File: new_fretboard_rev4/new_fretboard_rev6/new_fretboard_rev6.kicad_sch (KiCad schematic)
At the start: 0 parts

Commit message: two channels done
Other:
- added sheet ch2 (../new_fretboard_rev4/new_fretboard_rev4.kicad_sch)
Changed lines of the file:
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@@
 	(paper "A4")
 	(sheet
-		(at 54.61 27.94)
-		(size 25.4 17.78)
+		(at 29.21 27.94)
+		(size 22.86 13.97)
 		(exclude_from_sim no)
 		(in_bom yes)
@@
 		)
 		(property "Sheetname" "ch1"
-			(at 54.61 27.2284 0)
+			(at 29.21 27.2284 0)
 			(show_name no)
 			(do_not_autoplace no)
@@
 		)
 		(property "Sheetfile" "../new_fretboard_rev4/new_fretboard_rev4.kicad_sch"
-			(at 54.61 46.3046 0)
+			(at 29.21 42.4946 0)
 			(show_name no)
 			(do_not_autoplace no)
@@
 				)
 			)
+		)
+	)
+	(sheet
+		(at 99.06 25.4)
+		(size 31.75 16.51)
+		(exclude_from_sim no)
+		(in_bom yes)
+		(on_board yes)
+		(dnp no)
+		(fields_autoplaced yes)
+		(stroke
+			(width 0.1524)
+			(type solid)
+		)
+		(fill
+			(color 0 0 0 0)
+		)
+		(property "Sheetname" "ch2"
+			(at 99.06 24.6884 0)
+			(show_name no)
+			(do_not_autoplace no)
+			(effects
+				(font
+					(size 1.27 1.27)
+				)
+				(justify left bottom)
+			)
+		)
+		(property "Sheetfile" "../new_fretboard_rev4/new_fretboard_rev4.kicad_sch"
+			(at 99.06 42.4946 0)
+			(show_name no)
+			(do_not_autoplace no)
+			(effects
+				(font
+					(size 1.27 1.27)
+				)
+				(justify left top)
+			)
+		)
+		(instances
+			(project "new_fretboard_rev6"
+				(path "/0062b2a7-78dc-4b3a-83d1-c8e3134dc888"
+					(page "3")
+				)
+			)

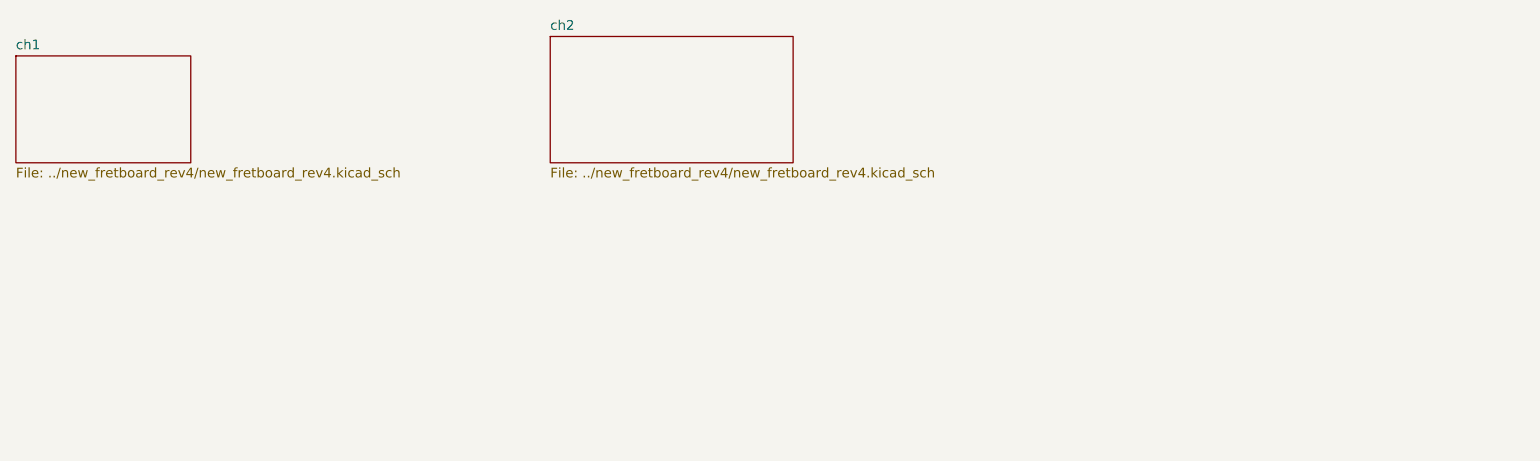
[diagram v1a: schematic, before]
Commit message: fully routed all channels, about to add tilts
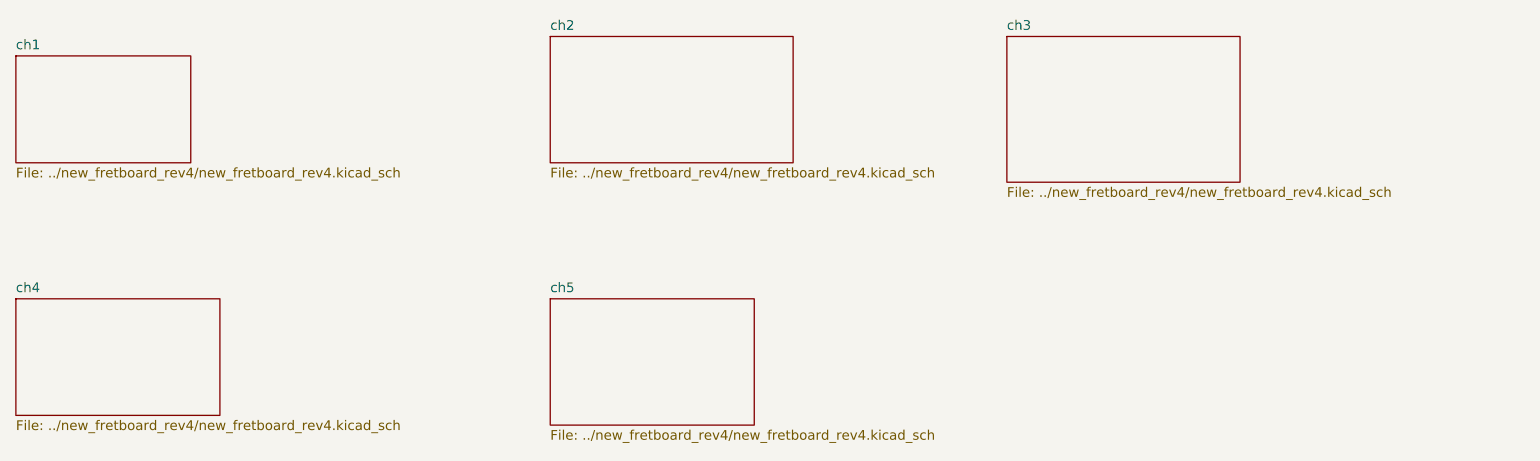
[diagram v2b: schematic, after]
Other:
- added sheet ch3 (../new_fretboard_rev4/new_fretboard_rev4.kicad_sch)
- added sheet ch4 (../new_fretboard_rev4/new_fretboard_rev4.kicad_sch)
- added sheet ch5 (../new_fretboard_rev4/new_fretboard_rev4.kicad_sch)
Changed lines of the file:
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@@
 	(paper "A4")
+	(sheet
+		(at 99.06 59.69)
+		(size 26.67 16.51)
+		(exclude_from_sim no)
+		(in_bom yes)
+		(on_board yes)
+		(dnp no)
+		(fields_autoplaced yes)
+		(stroke
+			(width 0.1524)
+			(type solid)
+		)
+		(fill
+			(color 0 0 0 0)
+		)
+		(property "Sheetname" "ch5"
+			(at 99.06 58.9784 0)
+			(show_name no)
+			(do_not_autoplace no)
+			(effects
+				(font
+					(size 1.27 1.27)
+				)
+				(justify left bottom)
+			)
+		)
+		(property "Sheetfile" "../new_fretboard_rev4/new_fretboard_rev4.kicad_sch"
+			(at 99.06 76.7846 0)
+			(show_name no)
+			(do_not_autoplace no)
+			(effects
+				(font
+					(size 1.27 1.27)
+				)
+				(justify left top)
+			)
+		)
+		(instances
+			(project "new_fretboard_rev6"
+				(path "/0062b2a7-78dc-4b3a-83d1-c8e3134dc888"
+					(page "6")
+				)
+			)
+		)
+	)
+	(sheet
+		(at 29.21 59.69)
+		(size 26.67 15.24)
+		(exclude_from_sim no)
+		(in_bom yes)
+		(on_board yes)
+		(dnp no)
+		(fields_autoplaced yes)
+		(stroke
+			(width 0.1524)
+			(type solid)
+		)
+		(fill
+			(color 0 0 0 0)
+		)
+		(property "Sheetname" "ch4"
+			(at 29.21 58.9784 0)
+			(show_name no)
+			(do_not_autoplace no)
+			(effects
+				(font
+					(size 1.27 1.27)
+				)
+				(justify left bottom)
+			)
+		)
+		(property "Sheetfile" "../new_fretboard_rev4/new_fretboard_rev4.kicad_sch"
+			(at 29.21 75.5146 0)
+			(show_name no)
+			(do_not_autoplace no)
+			(effects
+				(font
+					(size 1.27 1.27)
+				)
+				(justify left top)
+			)
+		)
+		(instances
+			(project "new_fretboard_rev6"
+				(path "/0062b2a7-78dc-4b3a-83d1-c8e3134dc888"
+					(page "5")
+				)
+			)
+		)
+	)
+	(sheet
+		(at 158.75 25.4)
+		(size 30.48 19.05)
+		(exclude_from_sim no)
+		(in_bom yes)
+		(on_board yes)
+		(dnp no)
+		(fields_autoplaced yes)
+		(stroke
+			(width 0.1524)
+			(type solid)
+		)
+		(fill
+			(color 0 0 0 0)
+		)
+		(property "Sheetname" "ch3"
+			(at 158.75 24.6884 0)
+			(show_name no)
+			(do_not_autoplace no)
+			(effects
+				(font
+					(size 1.27 1.27)
+				)
+				(justify left bottom)
+			)
+		)
+		(property "Sheetfile" "../new_fretboard_rev4/new_fretboard_rev4.kicad_sch"
+			(at 158.75 45.0346 0)
+			(show_name no)
+			(do_not_autoplace no)
+			(effects
+				(font
+					(size 1.27 1.27)
+				)
+				(justify left top)
+			)
+		)
+		(instances
+			(project "new_fretboard_rev6"
+				(path "/0062b2a7-78dc-4b3a-83d1-c8e3134dc888"
+					(page "4")
+				)
+			)
+		)
+	)
 	(sheet
 		(at 29.21 27.94)

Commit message: channels are done, working on microcontroller, daisy, and power junctions. getting heirarchical pin stuff sorted.
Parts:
- added J11: Conn_01x02_Pin, Connector_PinHeader_2.54mm:PinHeader_1x02_P2.54mm_Vertical, symbol Connector:Conn_01x02_Pin
- added J?: 110990030, Snapeda:SEEED_110990030, symbol Snapeda:110990030
- added U10: Daisy_Seed3, Module:Electrosmith_Daisy_Seed, symbol Snapeda:Daisy_Seed3
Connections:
- new net +5V: J?.1, J?.2
- new net GND1: J?.3, J?.4

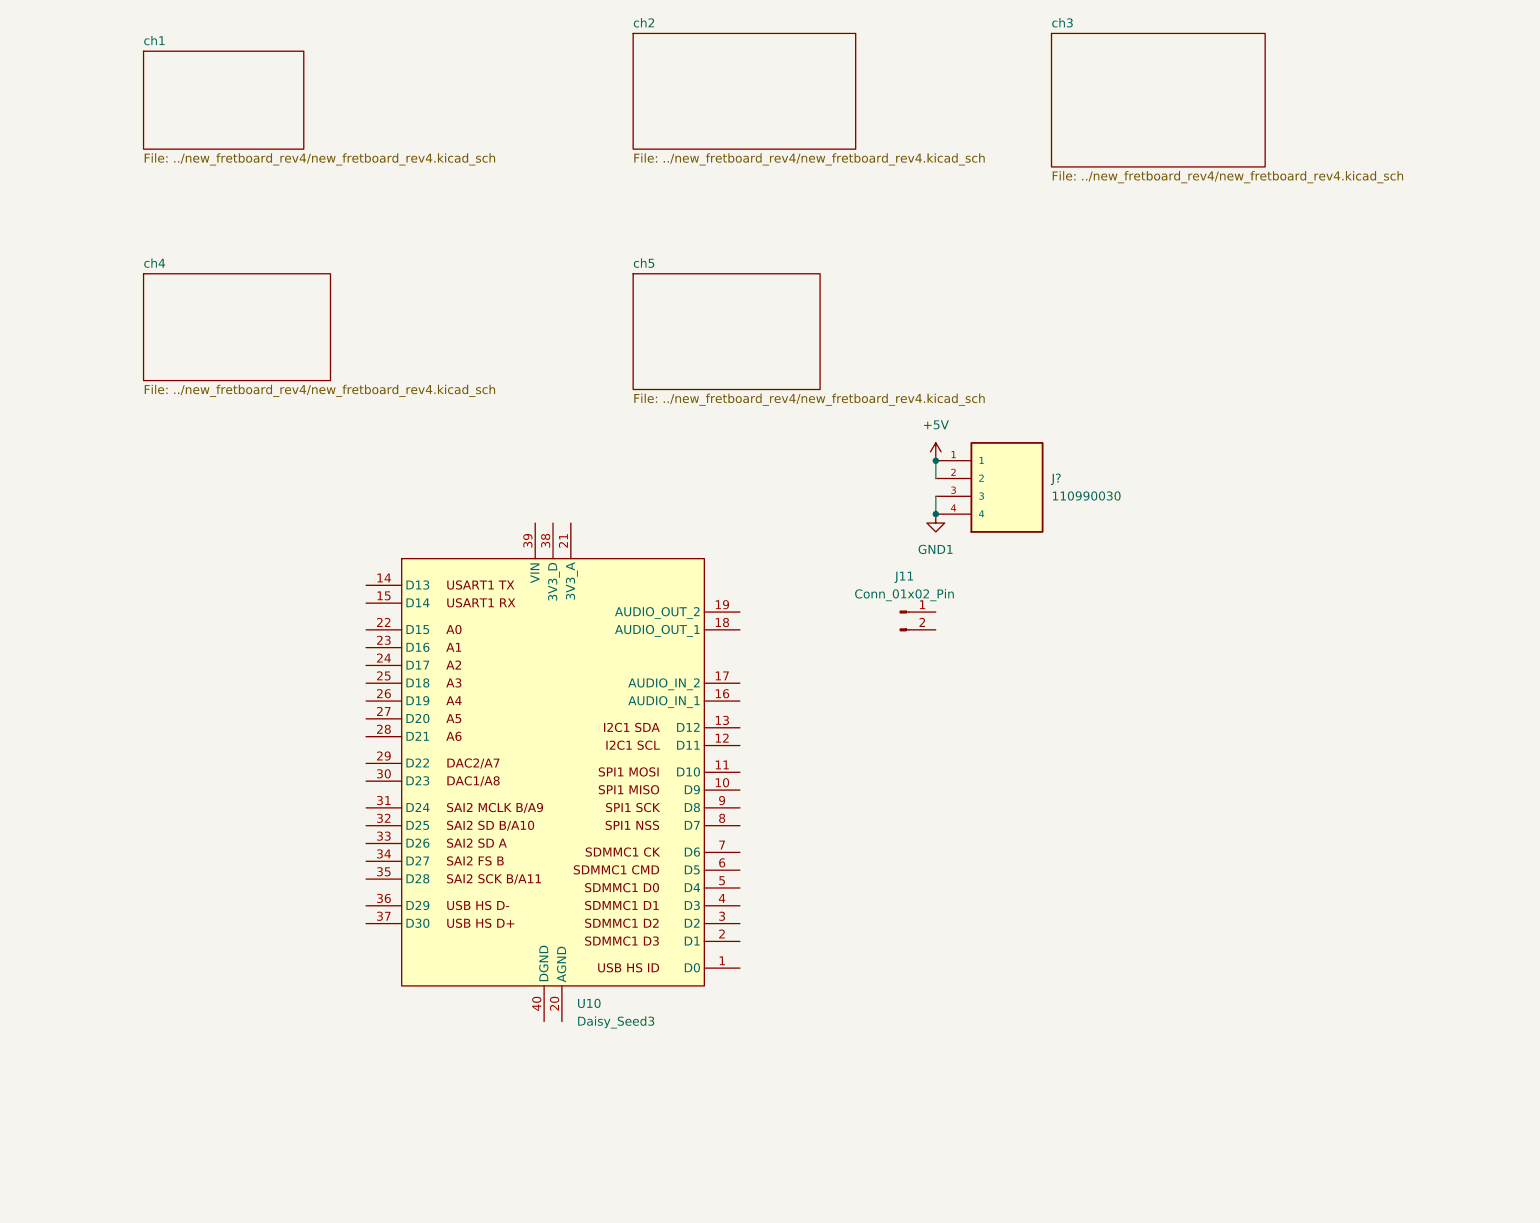
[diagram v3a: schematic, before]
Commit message: power in schematic, about to route power and sent wires
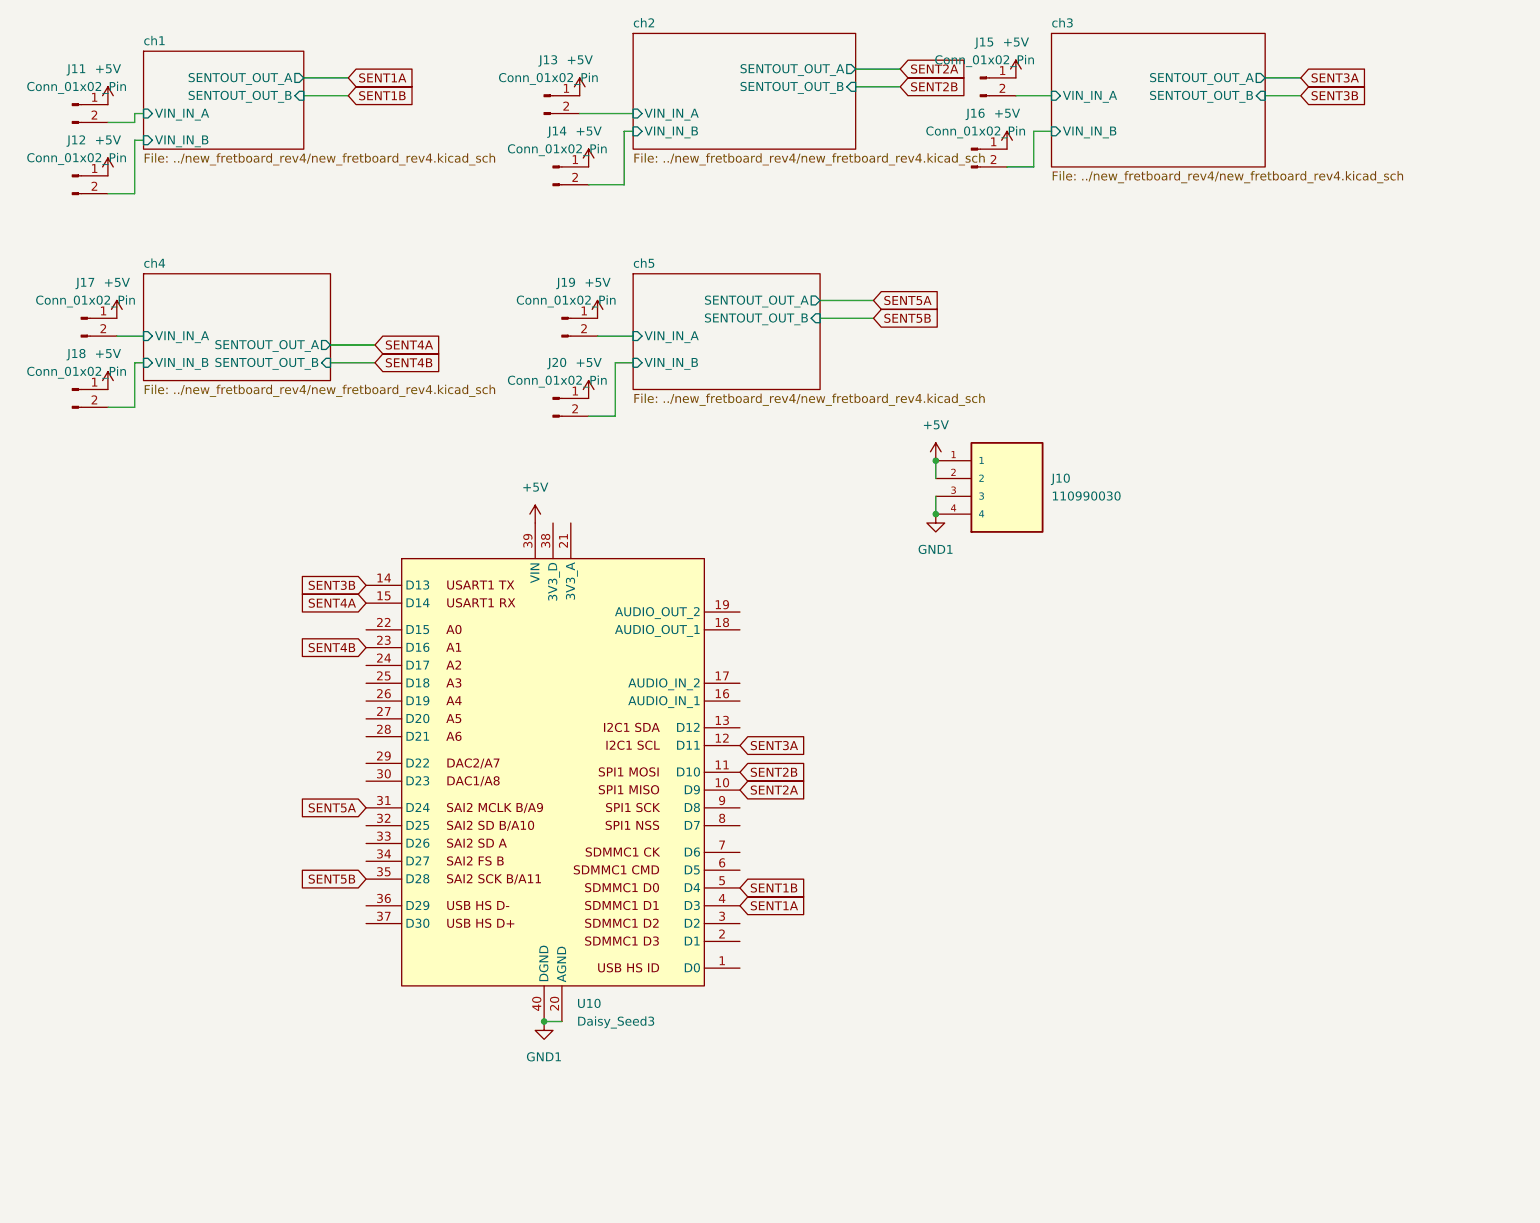
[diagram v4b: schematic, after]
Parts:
- added J12, J13, J14, J15, J16, J17, J18, J19, J20: Conn_01x02_Pin, Connector_PinHeader_2.54mm:PinHeader_1x02_P2.54mm_Vertical, symbol Connector:Conn_01x02_Pin
- gave numbers to parts that had none: 1
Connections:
- net +5V: now also J11.1 (Pin_1), U10.39 (VIN), J12.1 (Pin_1), J13.1 (Pin_1), J14.1 (Pin_1), J15.1 (Pin_1), J16.1 (Pin_1), J17.1 (Pin_1), J18.1 (Pin_1), J19.1 (Pin_1), J20.1 (Pin_1)
- net GND1: now also U10.20 (AGND), U10.40 (DGND)
- net SENT2A: now reaches U10.10 (D9)
- net SENT2B: now reaches U10.11 (D10)
- net SENT3A: now reaches U10.12 (D11)
- net SENT3B: now reaches U10.14 (D13)
- net SENT4A: now reaches U10.15 (D14)
- net SENT4B: now reaches U10.23 (D16)
- net SENT5A: now reaches U10.31 (D24)
- net SENT5B: now reaches U10.35 (D28)
- net SENT1A: now reaches U10.4 (D3)
- net SENT1B: now reaches U10.5 (D4)
- net ch1/VIN_IN_A: now reaches J11.2 (Pin_2)
- new net ch1/VIN_IN_B: J12.2 (Pin_2)
- new net ch2/VIN_IN_A: J13.2 (Pin_2)
- new net ch2/VIN_IN_B: J14.2 (Pin_2)
- new net ch3/VIN_IN_A: J15.2 (Pin_2)
- new net ch3/VIN_IN_B: J16.2 (Pin_2)
- new net ch4/VIN_IN_A: J17.2 (Pin_2)
- new net ch4/VIN_IN_B: J18.2 (Pin_2)
- new net ch5/VIN_IN_A: J19.2 (Pin_2)
- new net ch5/VIN_IN_B: J20.2 (Pin_2)
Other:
- sheet ch1 ports: added SENTOUT_OUT_A, SENTOUT_OUT_B, VIN_IN_A, VIN_IN_B; removed none
- sheet ch2 ports: added SENTOUT_OUT_A, SENTOUT_OUT_B, VIN_IN_A, VIN_IN_B; removed none
- sheet ch3 ports: added SENTOUT_OUT_A, SENTOUT_OUT_B, VIN_IN_A, VIN_IN_B; removed none
- sheet ch4 ports: added SENTOUT_OUT_A, SENTOUT_OUT_B, VIN_IN_A, VIN_IN_B; removed none
- sheet ch5 ports: added SENTOUT_OUT_A, SENTOUT_OUT_B, VIN_IN_A, VIN_IN_B; removed none
- moved on the sheet: J11

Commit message: everything except cleaning up silkscreen done
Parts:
- added H1, H2: MountingHole, MountingHole:MountingHole_3.2mm_M3, symbol Mechanical:MountingHole
- added H3, H4, H5, H6, H7, H8, H9: MountingHole, MountingHole:MountingHole_2.1mm, symbol Mechanical:MountingHole
- added J24: Conn_01x03_Pin, Connector_PinHeader_2.54mm:PinHeader_1x03_P2.54mm_Vertical, symbol Connector:Conn_01x03_Pin
- added J25: Conn_01x07_Pin, Connector_PinHeader_2.54mm:PinHeader_1x07_P2.54mm_Vertical, symbol Connector:Conn_01x07_Pin
- added J26: Conn_01x01_Pin, Connector_PinSocket_2.54mm:PinSocket_1x01_P2.54mm_Vertical, symbol Connector:Conn_01x01_Pin
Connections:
- net at U10.1 (D0): now also J24.1 (Pin_1)
- net at U10.13 (D12): now also J26.1 (Pin_1)
- net at U10.2 (D1): now also J24.2 (Pin_2)
- net at U10.24 (D17): now also J25.1 (Pin_1)
- net at U10.25 (D18): now also J25.2 (Pin_2)
- net at U10.26 (D19): now also J25.3 (Pin_3)
- net at U10.27 (D20): now also J25.4 (Pin_4)
- net at U10.28 (D21): now also J25.5 (Pin_5)
- net at U10.29 (D22): now also J25.6 (Pin_6)
- net at U10.3 (D2): now also J24.3 (Pin_3)
- net at U10.30 (D23): now also J25.7 (Pin_7)

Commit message: finished, about to export gerbers
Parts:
- added J27: Conn_01x03_Pin, Connector_PinHeader_2.54mm:PinHeader_1x03_P2.54mm_Vertical, symbol Connector:Conn_01x03_Pin
- added J28: Conn_01x01_Pin, Connector_PinSocket_2.54mm:PinSocket_1x01_P2.54mm_Vertical, symbol Connector:Conn_01x01_Pin
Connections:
- net +5V: now also J27.3 (Pin_3)
- net GND1: now also J27.1 (Pin_1), J27.2 (Pin_2), J28.1 (Pin_1)

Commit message: all routing fixed, just added power cap
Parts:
- added C101: 22uf, Capacitor_THT:CP_Radial_D10.0mm_P3.50mm, symbol Device:C_Polarized
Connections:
- net +5V: now also C101.1
- net GND1: now also C101.2
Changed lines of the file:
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@@
 	(wire
 		(pts
+			(xy 138.43 86.36) (xy 142.24 86.36)
+		)
+		(stroke
+			(width 0)
+			(type default)
+		)
+	)
+	(wire
+		(pts
 			(xy 125.73 66.04) (xy 133.35 66.04)
 		)
@@
 	(wire
 		(pts
+			(xy 138.43 93.98) (xy 142.24 93.98)
+		)
+		(stroke
+			(width 0)
+			(type default)
+		)
+	)
+	(wire
+		(pts
 			(xy 156.21 39.37) (xy 158.75 39.37)
 		)
@@
 					(unit 1)
 				)
+			)
+		)
+	)
+	(symbol
+		(lib_id "Device:C_Polarized")
+		(at 138.43 90.17 0)
+		(unit 1)
+		(body_style 1)
+		(exclude_from_sim no)
+		(in_bom yes)
+		(on_board yes)
+		(in_pos_files yes)
+		(dnp no)
+		(property "Reference" "C101"
+			(at 130.302 89.662 0)
+			(show_name no)
+			(do_not_autoplace no)
+			(effects
+				(font
+					(size 1.27 1.27)
+				)
+				(justify left)
+			)
+		)
+		(property "Value" "22uf"
+			(at 130.81 87.63 0)
+			(show_name no)
+			(do_not_autoplace no)
+			(effects
+				(font
+					(size 1.27 1.27)
+				)
+				(justify left)
+			)
+		)
+		(property "Footprint" "Capacitor_THT:CP_Radial_D10.0mm_P3.50mm"
+			(at 139.3952 93.98 0)
+			(hide yes)
+			(show_name no)
+			(do_not_autoplace no)
+			(effects
+				(font
+					(size 1.27 1.27)
+				)
+			)
+		)
+		(property "Datasheet" ""
+			(at 138.43 90.17 0)
+			(hide yes)
+			(show_name no)
+			(do_not_autoplace no)
+			(effects
+				(font
+					(size 1.27 1.27)
+				)
+			)
+		)
+		(property "Description" "Polarized capacitor"
+			(at 138.43 90.17 0)
+			(hide yes)
+			(show_name no)
+			(do_not_autoplace no)
+			(effects
+				(font
+					(size 1.27 1.27)
+				)
+			)
+		)
+		(pin "2"
+		)
+		(pin "1"
+		)
+		(instances
+			(project "new_fretboard_rev6"
+				(path "/0062b2a7-78dc-4b3a-83d1-c8e3134dc888"
+					(reference "C101")
+					(unit 1)
+				)

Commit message: revision 6.1 finished
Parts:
- added C102: 1uf, Capacitor_SMD:C_1206_3216Metric, symbol Device:C
- C101: footprint Capacitor_THT:CP_Radial_D10.0mm_P3.50mm -> Capacitor_SMD:C_1210_3225Metric
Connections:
- net +5V: now also C102.1
- net GND1: now also C102.2
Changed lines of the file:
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@@
 	(paper "A4")
 	(junction
+		(at 138.43 86.36)
+		(diameter 0)
+		(color 0 0 0 0)
+	)
+	(junction
 		(at 142.24 86.36)
 		(diameter 0)
@@
 		(color 0 0 0 0)
 	)
+	(junction
+		(at 138.43 93.98)
+		(diameter 0)
+		(color 0 0 0 0)
+	)
 	(wire
 		(pts
@@
 	(wire
 		(pts
+			(xy 120.65 93.98) (xy 138.43 93.98)
+		)
+		(stroke
+			(width 0)
+			(type default)
+		)
+	)
+	(wire
+		(pts
 			(xy 55.88 69.85) (xy 62.23 69.85)
 		)
@@
 	(wire
 		(pts
+			(xy 138.43 86.36) (xy 120.65 86.36)
+		)
+		(stroke
+			(width 0)
+			(type default)
+		)
+	)
+	(wire
+		(pts
 			(xy 46.99 129.54) (xy 46.99 128.27)
 		)
@@
 	)
 	(symbol
+		(lib_id "Device:C")
+		(at 120.65 90.17 0)
+		(unit 1)
+		(body_style 1)
+		(exclude_from_sim no)
+		(in_bom yes)
+		(on_board yes)
+		(in_pos_files yes)
+		(dnp no)
+		(fields_autoplaced yes)
+		(property "Reference" "C102"
+			(at 124.46 88.8999 0)
+			(show_name no)
+			(do_not_autoplace no)
+			(effects
+				(font
+					(size 1.27 1.27)
+				)
+				(justify left)
+			)
+		)
+		(property "Value" "1uf"
+			(at 124.46 91.4399 0)
+			(show_name no)
+			(do_not_autoplace no)
+			(effects
+				(font
+					(size 1.27 1.27)
+				)
+				(justify left)
+			)
+		)
+		(property "Footprint" "Capacitor_SMD:C_1206_3216Metric"
+			(at 121.6152 93.98 0)
+			(hide yes)
+			(show_name no)
+			(do_not_autoplace no)
+			(effects
+				(font
+					(size 1.27 1.27)
+				)
+			)
+		)
+		(property "Datasheet" ""
+			(at 120.65 90.17 0)
+			(hide yes)
+			(show_name no)
+			(do_not_autoplace no)
+			(effects
+				(font
+					(size 1.27 1.27)
+				)
+			)
+		)
+		(property "Description" "Unpolarized capacitor"
+			(at 120.65 90.17 0)
+			(hide yes)
+			(show_name no)
+			(do_not_autoplace no)
+			(effects
+				(font
+					(size 1.27 1.27)
+				)
+			)
+		)
+		(pin "1"
+		)
+		(pin "2"
+		)
+		(instances
+			(project "new_fretboard_rev6"
+				(path "/0062b2a7-78dc-4b3a-83d1-c8e3134dc888"
+					(reference "C102")
+					(unit 1)
+				)
+			)
+		)
+	)
+	(symbol
 		(lib_id "Connector:Conn_01x02_Pin")
 		(at 19.05 45.72 0)
@@
 			)
 		)
-		(property "Footprint" "Capacitor_THT:CP_Radial_D10.0mm_P3.50mm"
+		(property "Footprint" "Capacitor_SMD:C_1210_3225Metric"
 			(at 139.3952 93.98 0)
 			(hide yes)
